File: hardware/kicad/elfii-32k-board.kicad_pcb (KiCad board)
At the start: 2 copper layers, 177.8 x 127.1 mm, 15 parts, among them J1 ELFII_86_MECH_UNVERIFIED, U1 74HCT273, U2 62256, U3 74HCT04, U4 74HCT86, U5 74HCT32

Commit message: Add routed D1 path between edge contact 58 and SRAM pin 12 using six plated vias; pending real KiCad DRC
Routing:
- net /D1: track 0.00 -> 97.7 mm, vias 0 -> 6
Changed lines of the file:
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@@
 (segment (start 145.5 95.76) (end 145.5 88.51) (width 0.3) (layer "F.Cu") (net 18))
 (segment (start 135.81 108.46) (end 135.81 105.92) (width 0.3) (layer "F.Cu") (net 18))
+(segment (start 102.5525 148.717) (end 101.2825 147.447) (width 0.254) (layer "F.Cu") (net 10))
+(segment (start 101.2825 147.447) (end 97.4725 143.637) (width 0.254) (layer "B.Cu") (net 10))
+(segment (start 97.4725 143.637) (end 96.52 143.637) (width 0.254) (layer "B.Cu") (net 10))
+(segment (start 96.52 143.637) (end 96.52 142.367) (width 0.254) (layer "B.Cu") (net 10))
+(segment (start 96.52 142.367) (end 115.2525 123.6345) (width 0.254) (layer "B.Cu") (net 10))
+(segment (start 115.2525 123.6345) (end 117.7925 121.0945) (width 0.254) (layer "F.Cu") (net 10))
+(segment (start 117.7925 121.0945) (end 121.92 116.967) (width 0.254) (layer "B.Cu") (net 10))
+(segment (start 121.92 116.967) (end 121.92 115.062) (width 0.254) (layer "B.Cu") (net 10))
+(segment (start 121.92 115.062) (end 122.555 114.427) (width 0.254) (layer "B.Cu") (net 10))
+(segment (start 122.555 114.427) (end 122.555 112.522) (width 0.254) (layer "B.Cu") (net 10))
+(segment (start 122.555 112.522) (end 122.8725 112.2045) (width 0.254) (layer "B.Cu") (net 10))
+(segment (start 122.8725 112.2045) (end 122.8725 105.2195) (width 0.254) (layer "B.Cu") (net 10))
+(segment (start 122.8725 105.2195) (end 123.19 104.902) (width 0.254) (layer "F.Cu") (net 10))
+(segment (start 123.19 104.902) (end 123.19 104.267) (width 0.254) (layer "F.Cu") (net 10))
+(segment (start 123.19 104.267) (end 123.825 103.632) (width 0.254) (layer "F.Cu") (net 10))
+(segment (start 123.825 103.632) (end 123.825 101.092) (width 0.254) (layer "F.Cu") (net 10))
+(segment (start 123.825 101.092) (end 125.73 99.187) (width 0.254) (layer "F.Cu") (net 10))
+(segment (start 125.73 99.187) (end 125.73 89.027) (width 0.254) (layer "F.Cu") (net 10))
+(segment (start 125.73 89.027) (end 127.635 89.027) (width 0.254) (layer "F.Cu") (net 10))
+(segment (start 127.635 89.027) (end 127.9525 88.7095) (width 0.254) (layer "F.Cu") (net 10))
+(segment (start 127.9525 88.7095) (end 129.2225 87.4395) (width 0.254) (layer "B.Cu") (net 10))
+(segment (start 129.2225 87.4395) (end 129.2225 86.8045) (width 0.254) (layer "B.Cu") (net 10))
+(segment (start 129.2225 86.8045) (end 129.54 87.122) (width 0.254) (layer "F.Cu") (net 10))
+(segment (start 129.54 87.122) (end 137.16 87.122) (width 0.254) (layer "F.Cu") (net 10))
+(segment (start 137.16 87.122) (end 137.4775 86.8045) (width 0.254) (layer "F.Cu") (net 10))
+(segment (start 137.4775 86.8045) (end 137.795 86.8045) (width 0.254) (layer "F.Cu") (net 10))
+(segment (start 137.795 86.8045) (end 138.1125 86.487) (width 0.254) (layer "F.Cu") (net 10))
+(segment (start 138.1125 86.487) (end 138.7475 86.487) (width 0.254) (layer "F.Cu") (net 10))
+(segment (start 138.7475 86.487) (end 139.065 86.1695) (width 0.254) (layer "F.Cu") (net 10))
+(segment (start 139.065 86.1695) (end 139.3825 86.1695) (width 0.254) (layer "F.Cu") (net 10))
+(segment (start 139.3825 86.1695) (end 139.7 85.852) (width 0.254) (layer "F.Cu") (net 10))
+(segment (start 139.7 85.852) (end 140.0175 85.852) (width 0.254) (layer "F.Cu") (net 10))
+(segment (start 140.0175 85.852) (end 140.335 85.5345) (width 0.254) (layer "F.Cu") (net 10))
+(segment (start 140.335 85.5345) (end 140.6525 85.5345) (width 0.254) (layer "F.Cu") (net 10))
+(segment (start 140.6525 85.5345) (end 140.97 85.217) (width 0.254) (layer "F.Cu") (net 10))
+(segment (start 140.97 85.217) (end 141.2875 85.217) (width 0.254) (layer "F.Cu") (net 10))
+(segment (start 141.2875 85.217) (end 141.605 84.8995) (width 0.254) (layer "F.Cu") (net 10))
+(segment (start 141.605 84.8995) (end 142.24 84.8995) (width 0.254) (layer "F.Cu") (net 10))
+(segment (start 142.24 84.8995) (end 142.5575 84.582) (width 0.254) (layer "F.Cu") (net 10))
+(segment (start 142.5575 84.582) (end 142.875 84.582) (width 0.254) (layer "F.Cu") (net 10))
+(segment (start 142.875 84.582) (end 143.1925 84.2645) (width 0.254) (layer "F.Cu") (net 10))
+(segment (start 143.1925 84.2645) (end 143.51 84.2645) (width 0.254) (layer "F.Cu") (net 10))
+(segment (start 143.51 84.2645) (end 143.8275 83.947) (width 0.254) (layer "F.Cu") (net 10))
+(segment (start 143.8275 83.947) (end 144.145 83.947) (width 0.254) (layer "F.Cu") (net 10))
+(segment (start 144.145 83.947) (end 144.4625 83.6295) (width 0.254) (layer "F.Cu") (net 10))
+(segment (start 144.4625 83.6295) (end 145.0975 83.6295) (width 0.254) (layer "F.Cu") (net 10))
+(segment (start 145.0975 83.6295) (end 145.415 83.312) (width 0.254) (layer "F.Cu") (net 10))
+(segment (start 102.4636 148.7424) (end 102.5525 148.717) (width 0.254) (layer "F.Cu") (net 10))
+(segment (start 145.415 83.312) (end 145.38 83.43) (width 0.254) (layer "F.Cu") (net 10))
+(via (at 101.2825 147.447) (size 0.6) (drill 0.3) (layers "F.Cu" "B.Cu") (net 10))
+(via (at 115.2525 123.6345) (size 0.6) (drill 0.3) (layers "F.Cu" "B.Cu") (net 10))
+(via (at 117.7925 121.0945) (size 0.6) (drill 0.3) (layers "F.Cu" "B.Cu") (net 10))
+(via (at 122.8725 105.2195) (size 0.6) (drill 0.3) (layers "F.Cu" "B.Cu") (net 10))
+(via (at 127.9525 88.7095) (size 0.6) (drill 0.3) (layers "F.Cu" "B.Cu") (net 10))
+(via (at 129.2225 86.8045) (size 0.6) (drill 0.3) (layers "F.Cu" "B.Cu") (net 10))
 (zone (net 18) (net_name "/GND") (layer "F.Cu")
 (hatch edge 0.508)

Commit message: Revert D1 trace that shorts unassigned edge fingers and three crossing GND straps; restore zero-short routing baseline
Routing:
- net /D1: track 97.7 -> 0.00 mm, vias 6 -> 0
- net /GND: track 24.7 -> 6.50 mm
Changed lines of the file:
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@@
 (gr_text "HIGH" (at 200 85.08 0) (layer "F.SilkS") (effects (font (size 0.9 0.9) (thickness 0.14))))
 (gr_text "SHUNT = ENABLE" (at 194 115 0) (layer "F.SilkS") (effects (font (size 0.85 0.85) (thickness 0.13))))
-(segment (start 74.5236 148.7424) (end 74.5236 140.335) (width 0.4) (layer "F.Cu") (net 18))
-(segment (start 145.5 95.76) (end 145.5 88.51) (width 0.3) (layer "F.Cu") (net 18))
-(segment (start 135.81 108.46) (end 135.81 105.92) (width 0.3) (layer "F.Cu") (net 18))
-(segment (start 102.5525 148.717) (end 101.2825 147.447) (width 0.254) (layer "F.Cu") (net 10))
-(segment (start 101.2825 147.447) (end 97.4725 143.637) (width 0.254) (layer "B.Cu") (net 10))
-(segment (start 97.4725 143.637) (end 96.52 143.637) (width 0.254) (layer "B.Cu") (net 10))
-(segment (start 96.52 143.637) (end 96.52 142.367) (width 0.254) (layer "B.Cu") (net 10))
-(segment (start 96.52 142.367) (end 115.2525 123.6345) (width 0.254) (layer "B.Cu") (net 10))
-(segment (start 115.2525 123.6345) (end 117.7925 121.0945) (width 0.254) (layer "F.Cu") (net 10))
-(segment (start 117.7925 121.0945) (end 121.92 116.967) (width 0.254) (layer "B.Cu") (net 10))
-(segment (start 121.92 116.967) (end 121.92 115.062) (width 0.254) (layer "B.Cu") (net 10))
-(segment (start 121.92 115.062) (end 122.555 114.427) (width 0.254) (layer "B.Cu") (net 10))
-(segment (start 122.555 114.427) (end 122.555 112.522) (width 0.254) (layer "B.Cu") (net 10))
-(segment (start 122.555 112.522) (end 122.8725 112.2045) (width 0.254) (layer "B.Cu") (net 10))
-(segment (start 122.8725 112.2045) (end 122.8725 105.2195) (width 0.254) (layer "B.Cu") (net 10))
-(segment (start 122.8725 105.2195) (end 123.19 104.902) (width 0.254) (layer "F.Cu") (net 10))
-(segment (start 123.19 104.902) (end 123.19 104.267) (width 0.254) (layer "F.Cu") (net 10))
-(segment (start 123.19 104.267) (end 123.825 103.632) (width 0.254) (layer "F.Cu") (net 10))
-(segment (start 123.825 103.632) (end 123.825 101.092) (width 0.254) (layer "F.Cu") (net 10))
-(segment (start 123.825 101.092) (end 125.73 99.187) (width 0.254) (layer "F.Cu") (net 10))
-(segment (start 125.73 99.187) (end 125.73 89.027) (width 0.254) (layer "F.Cu") (net 10))
-(segment (start 125.73 89.027) (end 127.635 89.027) (width 0.254) (layer "F.Cu") (net 10))
-(segment (start 127.635 89.027) (end 127.9525 88.7095) (width 0.254) (layer "F.Cu") (net 10))
-(segment (start 127.9525 88.7095) (end 129.2225 87.4395) (width 0.254) (layer "B.Cu") (net 10))
-(segment (start 129.2225 87.4395) (end 129.2225 86.8045) (width 0.254) (layer "B.Cu") (net 10))
-(segment (start 129.2225 86.8045) (end 129.54 87.122) (width 0.254) (layer "F.Cu") (net 10))
-(segment (start 129.54 87.122) (end 137.16 87.122) (width 0.254) (layer "F.Cu") (net 10))
-(segment (start 137.16 87.122) (end 137.4775 86.8045) (width 0.254) (layer "F.Cu") (net 10))
-(segment (start 137.4775 86.8045) (end 137.795 86.8045) (width 0.254) (layer "F.Cu") (net 10))
-(segment (start 137.795 86.8045) (end 138.1125 86.487) (width 0.254) (layer "F.Cu") (net 10))
-(segment (start 138.1125 86.487) (end 138.7475 86.487) (width 0.254) (layer "F.Cu") (net 10))
-(segment (start 138.7475 86.487) (end 139.065 86.1695) (width 0.254) (layer "F.Cu") (net 10))
-(segment (start 139.065 86.1695) (end 139.3825 86.1695) (width 0.254) (layer "F.Cu") (net 10))
-(segment (start 139.3825 86.1695) (end 139.7 85.852) (width 0.254) (layer "F.Cu") (net 10))
-(segment (start 139.7 85.852) (end 140.0175 85.852) (width 0.254) (layer "F.Cu") (net 10))
-(segment (start 140.0175 85.852) (end 140.335 85.5345) (width 0.254) (layer "F.Cu") (net 10))
-(segment (start 140.335 85.5345) (end 140.6525 85.5345) (width 0.254) (layer "F.Cu") (net 10))
-(segment (start 140.6525 85.5345) (end 140.97 85.217) (width 0.254) (layer "F.Cu") (net 10))
-(segment (start 140.97 85.217) (end 141.2875 85.217) (width 0.254) (layer "F.Cu") (net 10))
-(segment (start 141.2875 85.217) (end 141.605 84.8995) (width 0.254) (layer "F.Cu") (net 10))
-(segment (start 141.605 84.8995) (end 142.24 84.8995) (width 0.254) (layer "F.Cu") (net 10))
-(segment (start 142.24 84.8995) (end 142.5575 84.582) (width 0.254) (layer "F.Cu") (net 10))
-(segment (start 142.5575 84.582) (end 142.875 84.582) (width 0.254) (layer "F.Cu") (net 10))
-(segment (start 142.875 84.582) (end 143.1925 84.2645) (width 0.254) (layer "F.Cu") (net 10))
-(segment (start 143.1925 84.2645) (end 143.51 84.2645) (width 0.254) (layer "F.Cu") (net 10))
-(segment (start 143.51 84.2645) (end 143.8275 83.947) (width 0.254) (layer "F.Cu") (net 10))
-(segment (start 143.8275 83.947) (end 144.145 83.947) (width 0.254) (layer "F.Cu") (net 10))
-(segment (start 144.145 83.947) (end 144.4625 83.6295) (width 0.254) (layer "F.Cu") (net 10))
-(segment (start 144.4625 83.6295) (end 145.0975 83.6295) (width 0.254) (layer "F.Cu") (net 10))
-(segment (start 145.0975 83.6295) (end 145.415 83.312) (width 0.254) (layer "F.Cu") (net 10))
-(segment (start 102.4636 148.7424) (end 102.5525 148.717) (width 0.254) (layer "F.Cu") (net 10))
-(segment (start 145.415 83.312) (end 145.38 83.43) (width 0.254) (layer "F.Cu") (net 10))
-(via (at 101.2825 147.447) (size 0.6) (drill 0.3) (layers "F.Cu" "B.Cu") (net 10))
-(via (at 115.2525 123.6345) (size 0.6) (drill 0.3) (layers "F.Cu" "B.Cu") (net 10))
-(via (at 117.7925 121.0945) (size 0.6) (drill 0.3) (layers "F.Cu" "B.Cu") (net 10))
-(via (at 122.8725 105.2195) (size 0.6) (drill 0.3) (layers "F.Cu" "B.Cu") (net 10))
-(via (at 127.9525 88.7095) (size 0.6) (drill 0.3) (layers "F.Cu" "B.Cu") (net 10))
-(via (at 129.2225 86.8045) (size 0.6) (drill 0.3) (layers "F.Cu" "B.Cu") (net 10))
 (zone (net 18) (net_name "/GND") (layer "F.Cu")
 (hatch edge 0.508)

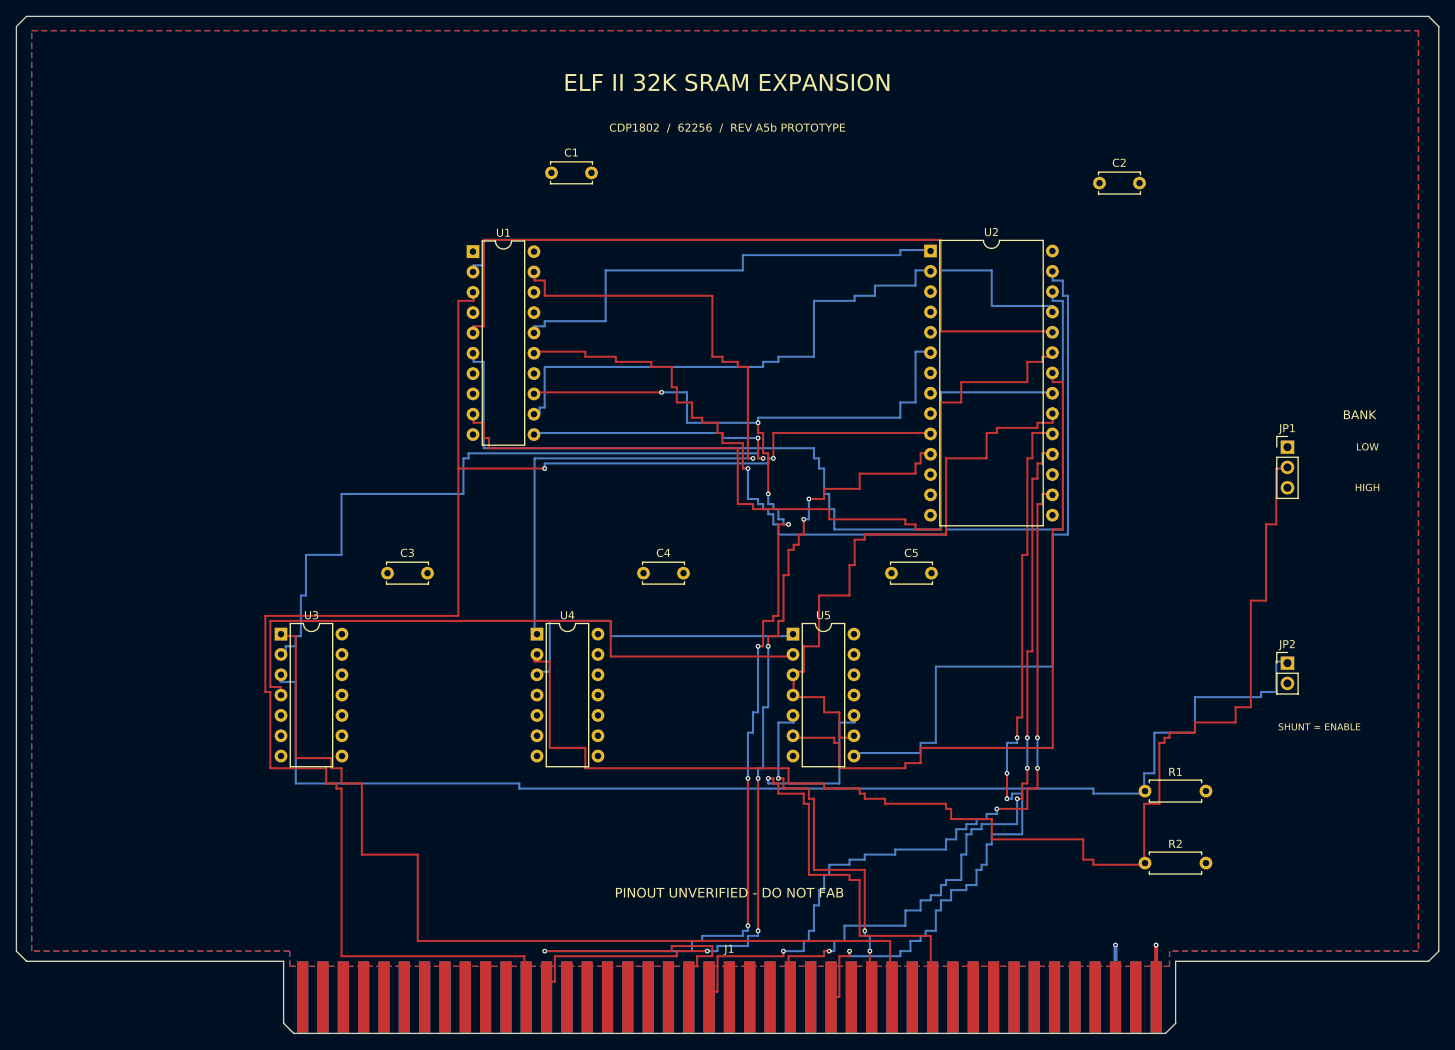
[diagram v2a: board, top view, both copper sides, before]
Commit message: Experimental full reroute of MA0-7, D0-7, TPA, NMRD and NMWR with all 86 edge fingers modeled as copper obstacles
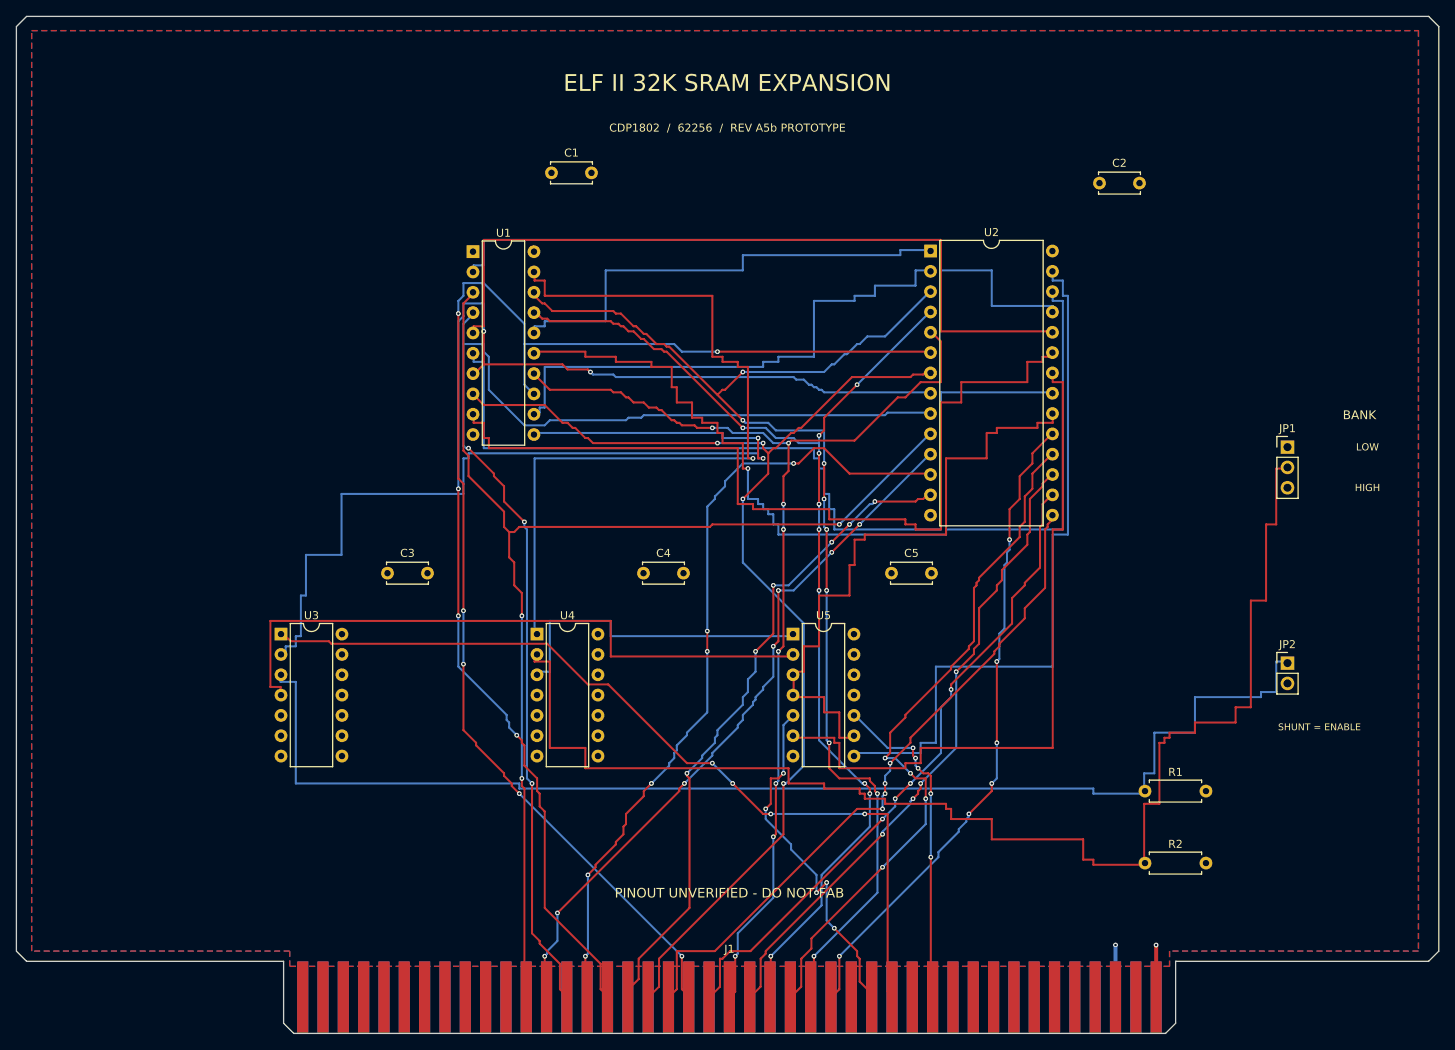
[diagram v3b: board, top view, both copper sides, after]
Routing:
- net /MA2: track 0.00 -> 164.3 mm, vias 0 -> 5
- net /MA1: track 0.00 -> 158.1 mm, vias 0 -> 3
- net /MA7: track 0.00 -> 155.1 mm, vias 0 -> 9
- net /MA3: track 0.00 -> 145.7 mm, vias 0 -> 4
- net /MA6: track 0.00 -> 142.1 mm, vias 0 -> 10
- net /MA5: track 0.00 -> 137.0 mm, vias 0 -> 8
- net /D1: track 0.00 -> 100.8 mm, vias 0 -> 6
- net /D3: track 0.00 -> 85.0 mm, vias 0 -> 4
- net /D2: track 0.00 -> 83.8 mm, vias 0 -> 6
- net /D5: track 0.00 -> 81.3 mm, vias 0 -> 4
- net /MA0: track 210.5 -> 150.0 mm, vias 2 -> 3
- net /D0: track 116.3 -> 89.4 mm, vias 6 -> 7
- net /NMWR: track 67.6 -> 41.7 mm, vias 1 -> 5
- net /D4: track 106.2 -> 82.5 mm
- net /D7: track 104.9 -> 82.1 mm, vias 4 -> 6
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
